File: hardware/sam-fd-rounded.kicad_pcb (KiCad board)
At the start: 4 copper layers, 36.4 x 55.2 mm, 70 parts, among them J1 Conn_ARM_JTAG_SWD_10, J2 USB_B_Micro, J3 DB9_Male_MountingHoles, SW1 SW_Push, U1 ATSAMC21E, U2 CP2102N-Axx-xQFN28, U3 TJA1443AT, U4 PESD2CANFD24L, Y1 32.768kHz, Y2 32MHz

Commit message: ordered, pray this works
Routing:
- net +5V: track 38.2 -> 37.4 mm
- net /MCU/SWCLK: track 18.4 -> 17.8 mm
- net /MCU/SWDIO: track 17.9 -> 17.4 mm

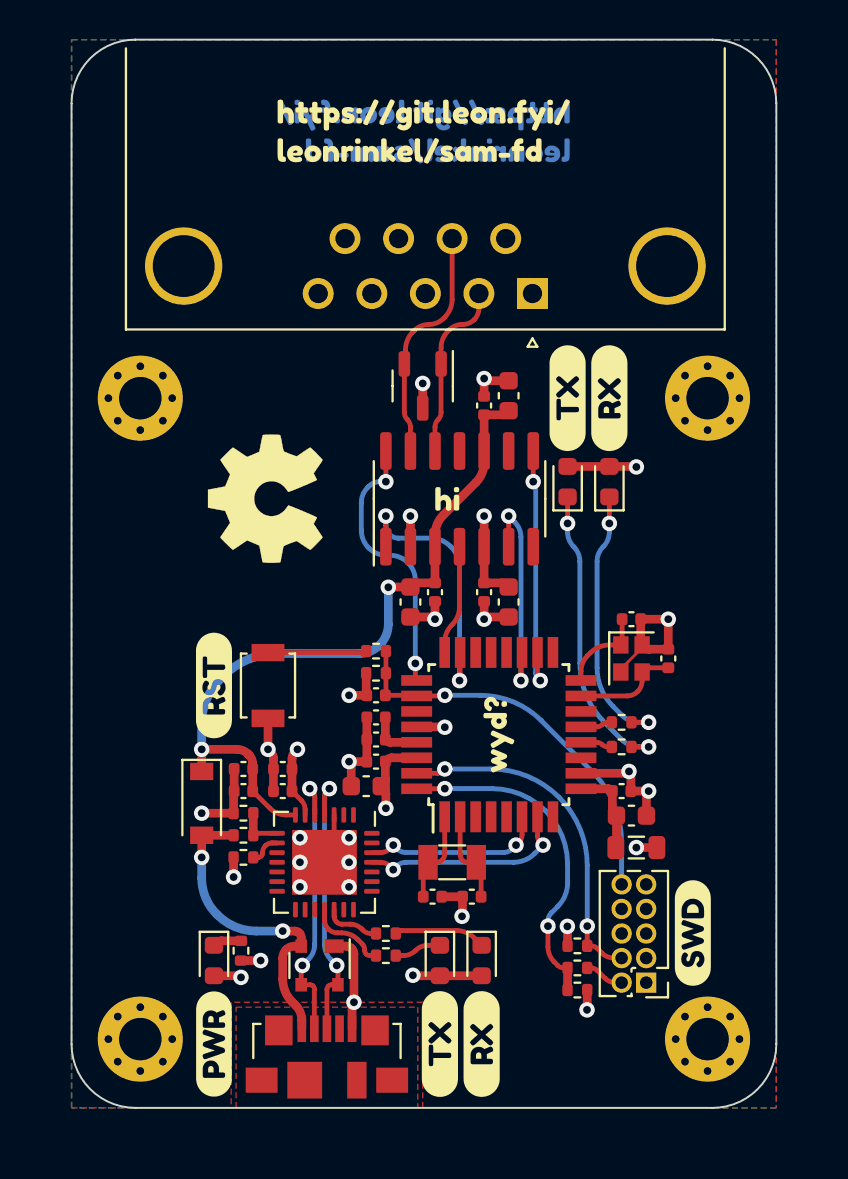
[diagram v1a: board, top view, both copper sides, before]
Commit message: leds through transistor, castellated holes
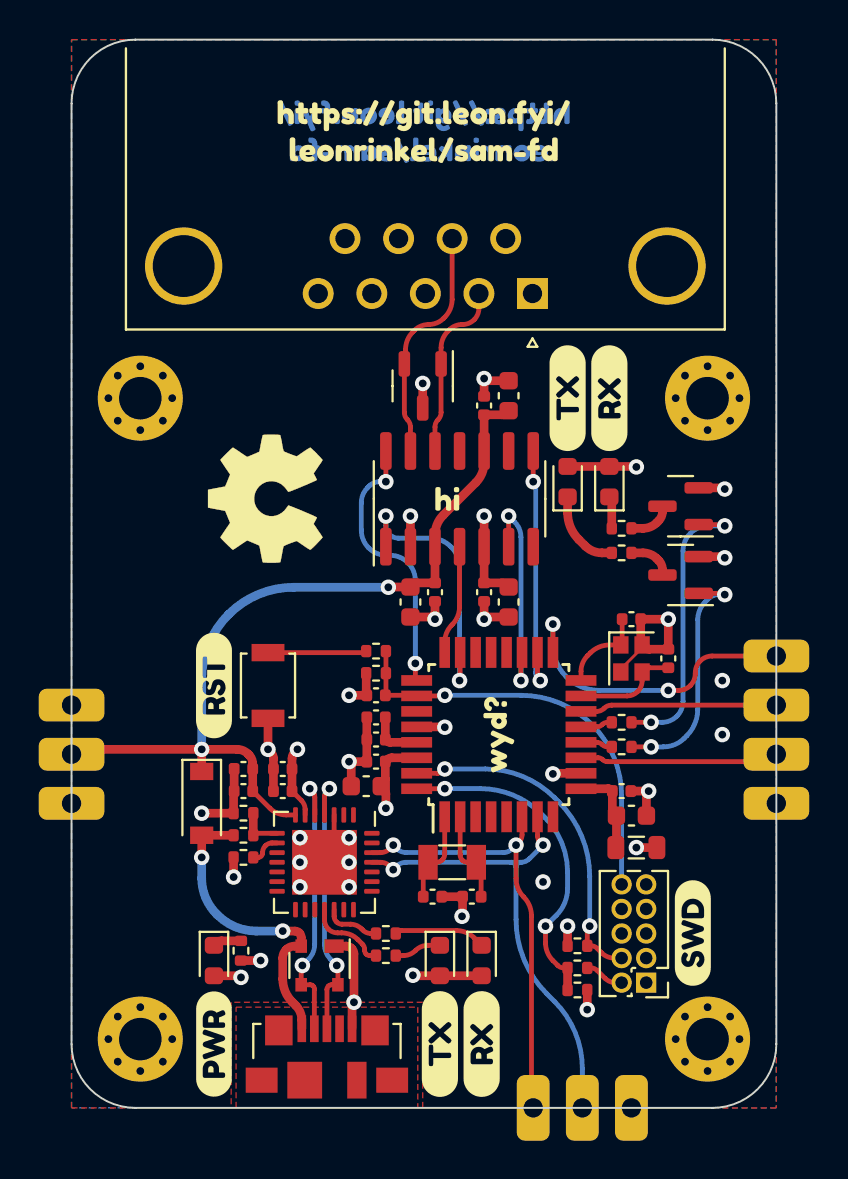
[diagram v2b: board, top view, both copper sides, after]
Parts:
- removed kibuzzard-63D40D4B: G***, kibuzzard-63D40D4B
- removed kibuzzard-63D40D8D (x2): G***, kibuzzard-63D40D8D
- added J4: Conn_01x04, sam-fd:CastellatedHoles_1x04_P2.54mm, F.Cu at (120.8, 82.2)
- added J5: Conn_01x03, sam-fd:CastellatedHoles_1x03_P2.54mm, F.Cu at (84.3, 77.1)
- added J6: Conn_01x03, sam-fd:CastellatedHoles_1x03_P2.54mm, F.Cu at (108.2, 97.9)
- added Q1: Q_NPN_BEC, Package_TO_SOT_SMD:SOT-23, F.Cu at (115.8, 70.4)
- added Q2: Q_NPN_BEC, Package_TO_SOT_SMD:SOT-23, F.Cu at (115.8, 66.8)
- added R14: 47.5kΩ, Resistor_SMD:R_0402_1005Metric, F.Cu at (110.5, 89.5)
- added R15: 47.5kΩ, Resistor_SMD:R_0402_1005Metric, F.Cu at (110.5, 91.8)
- added kibuzzard-63E7A195: G***, kibuzzard-63E7A195, F.Cu at (102.5, 46.6)
- added kibuzzard-63E7A1A7: G***, kibuzzard-63E7A1A7, F.Cu at (102.5, 48.4)
- added kibuzzard-63E7A1EC: G***, kibuzzard-63E7A1EC, F.Cu at (102.5, 46.6)
- added kibuzzard-63E7A1F6: G***, kibuzzard-63E7A1F6, F.Cu at (102.5, 48.4)
- added kibuzzard-63E7A25C: G***, kibuzzard-63E7A25C, B.Cu at (102.5, 46.6)
- added kibuzzard-63E7A280: G***, kibuzzard-63E7A280, B.Cu at (102.5, 48.4)
- R6, R7: value 33kΩ -> 10kΩ
- moved R7 14.0 mm to (112.8, 78.0)
- moved R6 10.5 mm to (112.8, 79.2), turned to 0 degrees
- moved R2 10.0 mm to (112.8, 69.2), turned to 0 degrees
- moved R3 10.0 mm to (112.8, 67.9), turned to 0 degrees
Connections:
- R2 pad 2: /TX_ACT -> Net-(Q1-Pad3)
- R3 pad 2: /RX_ACT -> Net-(Q2-Pad3)
- R6 pad 1: /MCU/SWCLK -> /TX_ACT
- R6 pad 2: +3V3 -> Net-(Q1-Pad1)
- R7 pad 1: /MCU/SWDIO -> /RX_ACT
- R7 pad 2: +3V3 -> Net-(Q2-Pad1)
- U1 pad 11: /MCU/PA08 -> /PA08
- U1 pad 14: /MCU/PA11 -> /PA11
- U1 pad 17: /MCU/PA16 -> /PA16
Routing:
- net /PA16: track 0.00 -> 16.4 mm, vias 0 -> 2
- net Net-(Q2-Pad1): track 0.00 -> 15.3 mm, vias 0 -> 2
- net /UART_TX: track 11.0 -> 25.2 mm
- net /UART_RX: track 9.41 -> 23.2 mm
- net Net-(Q1-Pad1): track 0.00 -> 12.7 mm, vias 0 -> 2
- net Net-(D3-Pad1): track 14.2 -> 1.67 mm, vias 2 -> 0
- net Net-(D2-Pad1): track 15.8 -> 4.28 mm, vias 2 -> 0
- net /PA08: track 0.00 -> 10.3 mm
- net /PA11: track 0.00 -> 10.2 mm
- net +5V: track 37.4 -> 44.4 mm
- net Net-(Q1-Pad3): track 0.00 -> 2.32 mm
- net Net-(Q2-Pad3): track 0.00 -> 2.32 mm
- net /MCU/~{RESET}: track 20.6 -> 22.0 mm
- net GND: track 47.7 -> 48.3 mm, vias 21 -> 26
